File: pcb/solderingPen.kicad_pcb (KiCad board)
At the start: 2 copper layers, 69 x 9 mm, 47 parts, among them CON1 +12V, CON2 jack_narrow_tht, CON3 GND, Q1 PDTC114ET, T1 IPD50P04P4-13, U1 STM32F070F6P6, U2 BTS5012SDA, U3 MCP6051T-E/OT, U4 L78L33ACUTR, U5 MAG3110

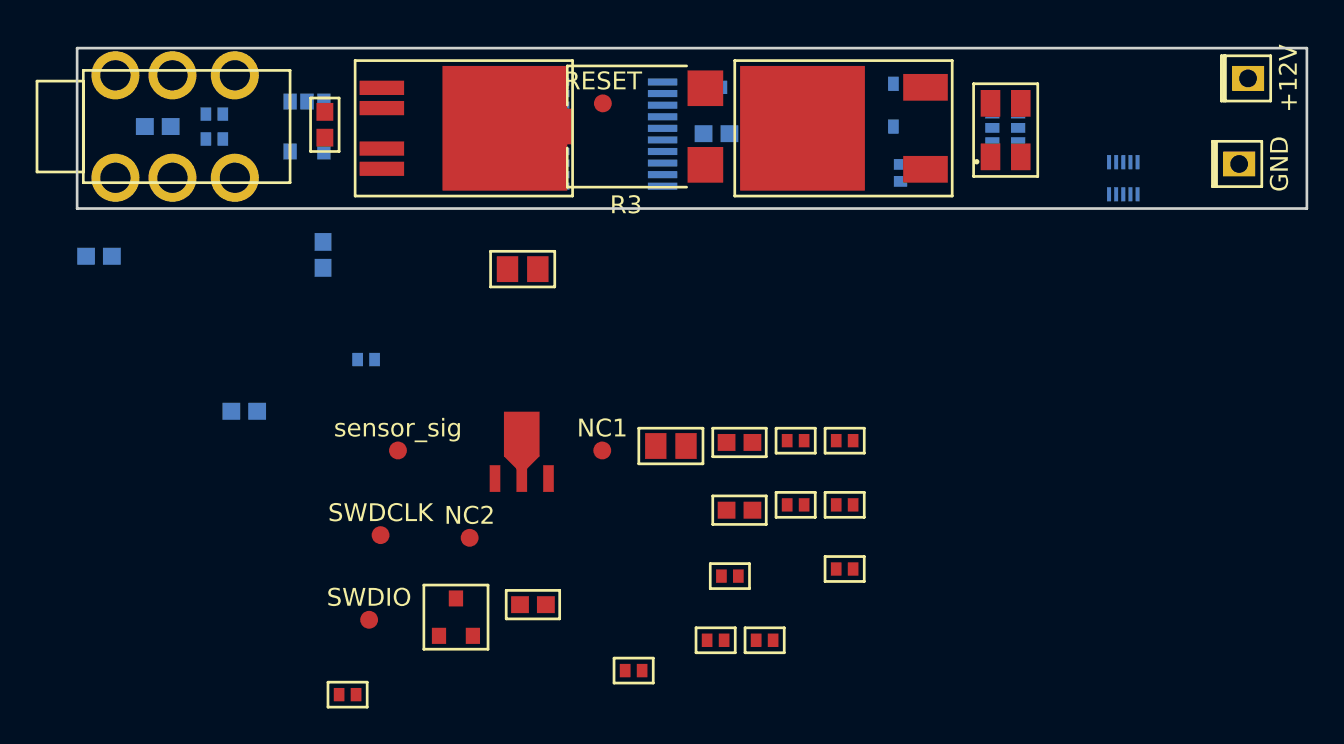
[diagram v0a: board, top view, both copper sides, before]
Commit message: Optimize uC pin assignments. Place components on PCB.
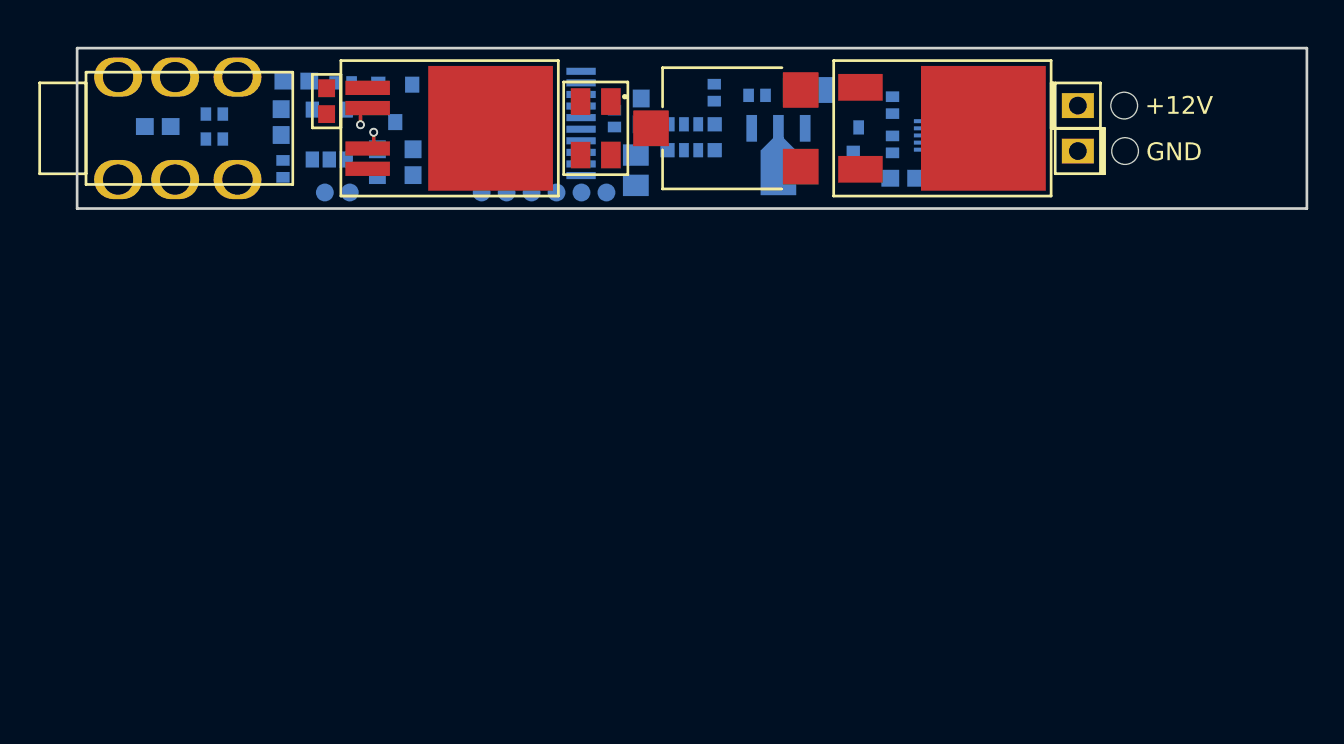
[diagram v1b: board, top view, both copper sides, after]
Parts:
- added C18: 100n, 0402_M, B.Cu at (124.4, 117.5)
- added REF**: mounting_hole_3.2_7.5_plated, niceMechanical:mounting_hole_3.2_7.5_plated, F.Cu at (168.3, 121.3)
- added REF**: mounting_hole_3.2_7.5_plated, niceMechanical:mounting_hole_3.2_7.5_plated, F.Cu at (168.2, 118.7)
- added TP7: GND, pnConnector:TP_1mm, B.Cu at (123.4, 123.6)
- added TP8: GND, pnConnector:TP_1mm, B.Cu at (139.2, 123.6)
- C10, C11, C12, C13, C14, C15, C16, C17, C3, C7, C8, C9, Q1, R10, R11, R4, TP1, TP2, TP3, TP4, TP5, TP6, U4: moved to B.Cu
- moved C3 39.5 mm to (145.2, 118.0), turned to 90 degrees
- moved C12 32.9 mm to (158.4, 122.7)
- moved R10 31.6 mm to (160.7, 119.8)
- moved R4 30.2 mm to (129.8, 117.7), turned to 90 degrees
- moved C8 29.8 mm to (139.7, 119.5), turned to 90 degrees
- moved Q1 29.0 mm to (127.3, 118.6)
- moved C7 28.3 mm to (141.2, 119.0), turned to 90 degrees
- moved C10 27.5 mm to (160.2, 121.5), turned to 270 degrees
- moved C16 27.0 mm to (147.7, 118.2)
- moved TP3 26.2 mm to (136.4, 123.6)
- moved C9 24.1 mm to (128.3, 121.9), turned to 270 degrees
- moved D2 23.0 mm to (138.6, 120.0), turned to 180 degrees
- moved C14 22.6 mm to (155.2, 118.7), turned to 90 degrees
- moved TP4 22.3 mm to (137.8, 123.6)
- moved R11 22.0 mm to (160.7, 118.3)
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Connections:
- RN1 pad 1: led_R_cmd -> led_B_cmd
- RN1 pad 2: led_G_cmd -> led_B_cmd
- RN1 pad 3: led_B_cmd -> led_G_cmd
- RN1 pad 4: led_B_cmd -> led_R_cmd
- RN1 pad 5: /led_B -> /led_R
- RN1 pad 6: /led_B -> /led_G
- RN1 pad 7: /led_G -> /led_B
- RN1 pad 8: /led_R -> /led_B
- U1 pad 10: sensor_sig -> driver_cmd
- U1 pad 11: (no net) -> potentiometer_sig
- U1 pad 17: driver_cmd -> SCL
- U1 pad 18: sensor_pullup_cmd -> SDA
- U1 pad 2: SDA -> /NC1
- U1 pad 3: SCL -> /NC2
- U1 pad 6: potentiometer_sig -> sensor_sig
- U1 pad 8: /NC1 -> sensor_pullup_cmd
- U1 pad 9: /NC2 -> (no net)
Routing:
- net Net-(Q1-Pad3): track 0.00 -> 2.16 mm, vias 0 -> 1
- net Net-(R4-Pad2): track 0.00 -> 1.18 mm, vias 0 -> 1
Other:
- copper layers 2 -> 4
- net class Default: clearance 0.2 -> 0.15; trace_width 0.25 -> 0.127; via_dia 0.6 -> 0.4572; via_drill 0.4 -> 0.254
- rule pad_to_mask_clearance: 0.2 -> 0.1
- rule trace_clearance: 0.2 -> 0.15
- rule trace_min: 0.2 -> 0.127
- rule via_min_drill: 0.3 -> 0.254
- rule via_min_size: 0.4 -> 0.4572

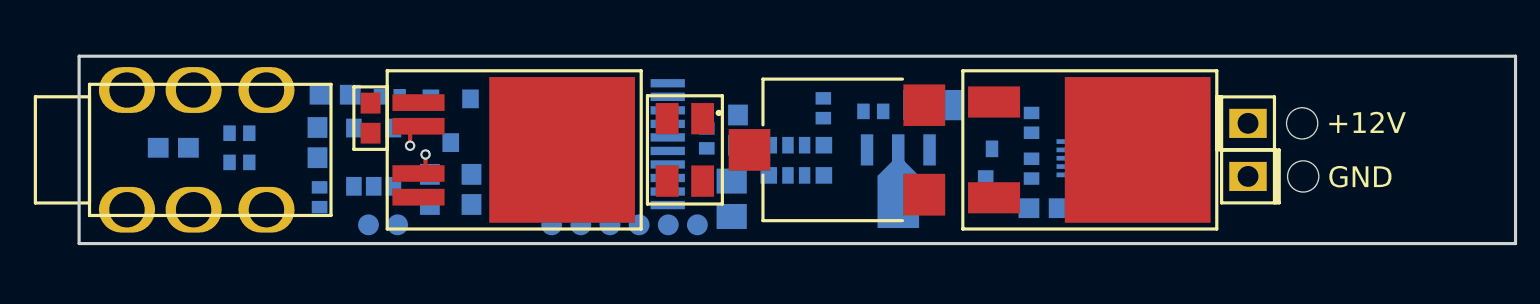
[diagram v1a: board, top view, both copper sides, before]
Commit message: Optimize uC pin assignments. Route PCB.
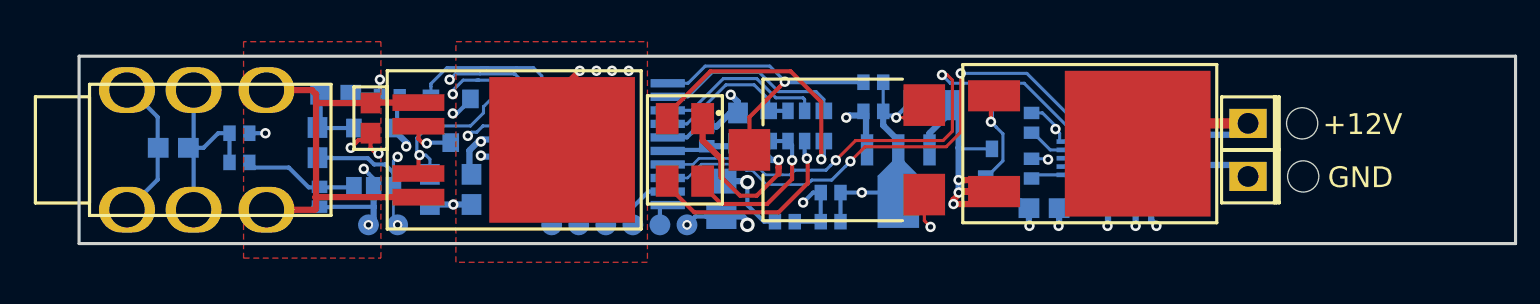
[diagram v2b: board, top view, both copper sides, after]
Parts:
- added C19: 100n, 0402_M, B.Cu at (145.6, 122.0)
- added R12: 10k, 0402_R_M, B.Cu at (143.4, 123.5)
- added R13: 100k, 0402_R_M, B.Cu at (145.6, 123.5)
- moved C3 2.71 mm to (147.7, 116.8), turned to 0 degrees
- moved R9 2.46 mm to (121.8, 117.3), turned to 180 degrees
- moved R8 2.45 mm to (121.0, 119.7), turned to 90 degrees
- moved RN1 1.65 mm to (143.9, 118.8)
- moved C17 0.50 mm to (140.3, 122.3)
- moved TP8 0.50 mm to (138.7, 123.6)
- moved TP4 0.40 mm to (137.4, 123.6)
- moved TP3 0.30 mm to (136.1, 123.6)
- moved T1 0.30 mm to (158.6, 119.7)
- moved TP1 0.20 mm to (134.8, 123.6)
- moved C8 0.10 mm to (139.7, 119.3)
- moved C7 0.10 mm to (141.2, 119.0)
- moved R4 0.10 mm to (129.8, 117.7)
- moved TP6 0.10 mm to (133.5, 123.6)
- turned CON1 to 180 degrees
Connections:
- U1 pad 6: sensor_sig -> vin_sense_sig
- U1 pad 9: (no net) -> sensor_sig
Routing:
- net GND: track 0.00 -> 156.4 mm, vias 0 -> 18
- net +3V3: track 0.00 -> 85.2 mm, vias 0 -> 7
- net +12V: track 0.00 -> 51.4 mm, vias 0 -> 8
- net SDA: track 0.00 -> 29.7 mm, vias 0 -> 2
- net SCL: track 0.00 -> 29.0 mm, vias 0 -> 2
- net vin_sense_sig: track 0.00 -> 26.0 mm, vias 0 -> 2
- net sensor_sig: track 0.00 -> 20.3 mm, vias 0 -> 3
- net /HEATER: track 0.00 -> 20.3 mm
- net sensor_pullup_cmd: track 0.00 -> 16.5 mm, vias 0 -> 2
- net potentiometer_sig: track 0.00 -> 14.1 mm, vias 0 -> 1
- net /led_R: track 0.00 -> 12.7 mm, vias 0 -> 1
- net /led_G: track 0.00 -> 10.2 mm, vias 0 -> 1
- net /SENSOR: track 0.00 -> 9.62 mm
- net led_R_cmd: track 0.00 -> 9.33 mm
- net /led_B: track 0.00 -> 8.33 mm, vias 0 -> 1
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- added copper zone on F.Cu, net +12V
- added copper zone on In1.Cu, net +12V
- added copper zone on In1.Cu, net +3V3
- added copper zone on F.Cu, net /HEATER
- added copper zone on In1.Cu, net GND
- added copper zone on In2.Cu, net GND

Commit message: Routing, step 2. Fix some components.
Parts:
- added REF**: mounting_hole_3.2_7.5_plated, niceMechanical:mounting_hole_3.2_7.5_plated, F.Cu at (112.5, 120.0)
- C15: footprint 0805_N -> solderingPen:0805_N
- D1: footprint SOD-323_N -> solderingPen:SOD-323_N
- R10: value 10k -> 4k7
- R12: value 10k -> 100k
- R13: value 100k -> 10k
- U1: footprint TSSOP-20_N -> solderingPen:TSSOP-20_N
- moved R12 1.31 mm to (142.4, 122.5)
- moved C4 1.03 mm to (115.0, 120.0)
- moved C19 0.95 mm to (144.7, 122.0)
- moved R13 0.95 mm to (144.7, 123.5)
- moved R7 0.46 mm to (117.7, 120.7)
- moved R6 0.46 mm to (117.7, 119.3)
- moved REF** 0.06 mm to (168.3, 118.8)
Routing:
- net GND: track 156.4 -> 158.6 mm, vias 18 -> 20
- net +12V: track 51.4 -> 49.8 mm
- net vin_sense_sig: track 26.0 -> 25.3 mm
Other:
- board size 69 x 9 mm -> 61 x 9 mm
- board text added: "C"
- board text added: "nicecircuits.com/solderingpen/"

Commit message: Finish PCB design.
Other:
- board text added: "v1.0"

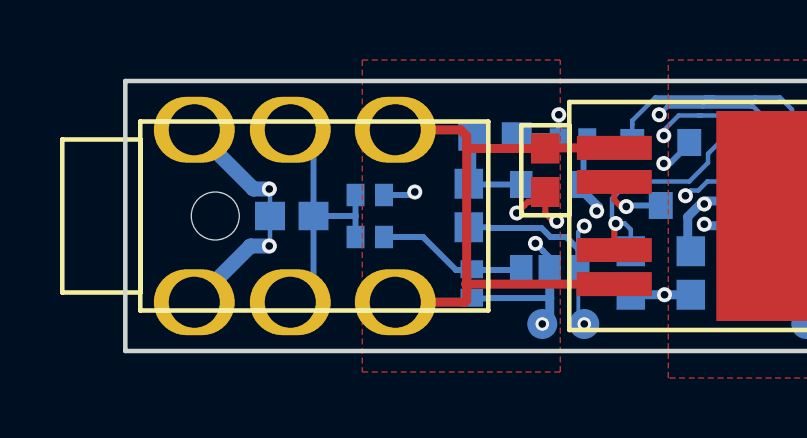
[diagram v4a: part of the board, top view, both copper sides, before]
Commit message: Update values of sensor amplifier resistors.
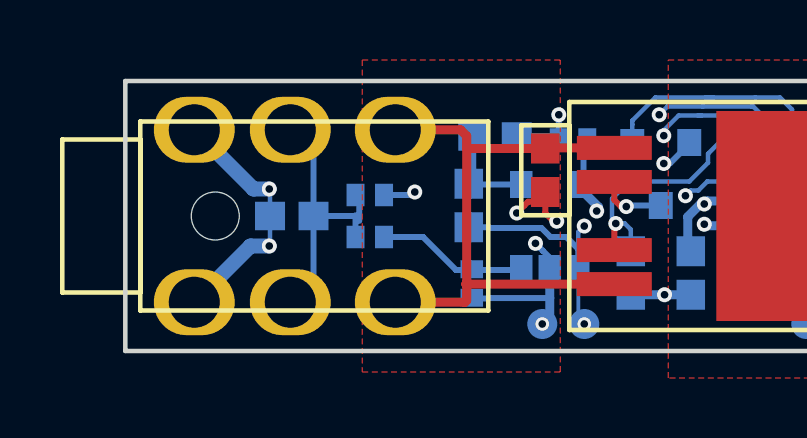
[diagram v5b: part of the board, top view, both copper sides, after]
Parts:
- R8: value R -> 18k
- R9: value R_V -> 100R
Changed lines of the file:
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@@
-(kicad_pcb (version 4) (host pcbnew 4.0.0-rc1-stable)
+(kicad_pcb (version 4) (host pcbnew 4.0.2-stable)
   (general
     (links 111)
-    (no_connects 0)
-    (area 105.599999 112.45 182.500001 126.000001)
+    (no_connects 1)
+    (area 109.424999 115.424999 170.575001 124.575001)
     (thickness 1.6)
     (drawings 16)
@@
   (page A4)
   (layers
-    (0 F.Cu signal)
-    (1 In1.Cu signal)
-    (2 In2.Cu signal)
+    (0 F.Cu signal hide)
+    (1 In1.Cu signal hide)
+    (2 In2.Cu signal hide)
     (31 B.Cu signal)
     (32 B.Adhes user hide)
@@
     (34 B.Paste user hide)
     (35 F.Paste user hide)
-    (36 B.SilkS user)
-    (37 F.SilkS user hide)
+    (36 B.SilkS user hide)
+    (37 F.SilkS user)
     (38 B.Mask user)
     (39 F.Mask user hide)
-    (40 Dwgs.User user hide)
+    (40 Dwgs.User user)
     (41 Cmts.User user)
     (42 Eco1.User user)
@@
     (44 Edge.Cuts user)
     (45 Margin user)
-    (46 B.CrtYd user)
-    (47 F.CrtYd user)
+    (46 B.CrtYd user hide)
+    (47 F.CrtYd user hide)
     (48 B.Fab user hide)
     (49 F.Fab user hide)
@@
     (solder_mask_min_width 0.1)
     (aux_axis_origin 0 0)
-    (visible_elements 7FFFFDBF)
+    (visible_elements 7FFFF5BF)
     (pcbplotparams
       (layerselection 0x010f0_80000007)
@@
       (effects (font (size 0.5 0.5) (thickness 0.05)) (justify mirror))
     )
-    (fp_text value R (at 0 -1.3 90) (layer B.Fab)
+    (fp_text value 18k (at 0 -1.3 90) (layer B.Fab)
       (effects (font (size 0.5 0.5) (thickness 0.05)) (justify mirror))
     )
@@
       (effects (font (size 0.5 0.5) (thickness 0.05)) (justify mirror))
     )
-    (fp_text value R_V (at 0 -1.3 180) (layer B.Fab)
+    (fp_text value 100R (at 0 -1.3 180) (layer B.Fab)
       (effects (font (size 0.5 0.5) (thickness 0.05)) (justify mirror))
     )
@@
   (segment (start 117.175 120.025) (end 117.175 120.7) (width 0.2) (layer B.Cu) (net 5))
   (segment (start 117.15 120) (end 117.175 119.975) (width 0.2) (layer B.Cu) (net 5))
-  (segment (start 117.175 119.975) (end 117.175 119.3) (width 0.2) (layer B.Cu) (net 5))
+  (segment (start 117.3 120.1625) (end 117.3 119.4875) (width 0.2) (layer B.Cu) (net 5))
   (segment (start 115.775 120) (end 117.15 120) (width 0.2) (layer B.Cu) (net 5))
   (segment (start 115.775 120) (end 115.775 122.1) (width 0.2) (layer B.Cu) (net 5))

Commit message: Update component values.
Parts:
- R7: value R -> 1k
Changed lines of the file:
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@@
       (effects (font (size 0.5 0.5) (thickness 0.05)) (justify mirror))
     )
-    (fp_text value R (at 0 -1.2 180) (layer B.Fab)
+    (fp_text value 1k (at 0 -1.2 180) (layer B.Fab)
       (effects (font (size 0.5 0.5) (thickness 0.05)) (justify mirror))
     )
